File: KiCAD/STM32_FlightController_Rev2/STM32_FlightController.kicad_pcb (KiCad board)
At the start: 4 copper layers, 42 x 44.4 mm, 54 parts, among them J1 USB_B_Micro, J10 Conn_01x08_Pin, J19 Conn_02x05_Odd_Even, J2 Conn_01x04_Pin, J3 Conn_01x04_Pin, SW1 PTS815SJM, SW2 SW_SPDT, U1 USBLC6-2SC6, U2 AMS1117-3.3, U3 TLV70018, U4 STM32F405RGTx, U5 BMP390L, U6 ICM-20948, U7 SN74LVC1T45DBV, U8 SN74LVC1T45DBV, Y1 8MHz

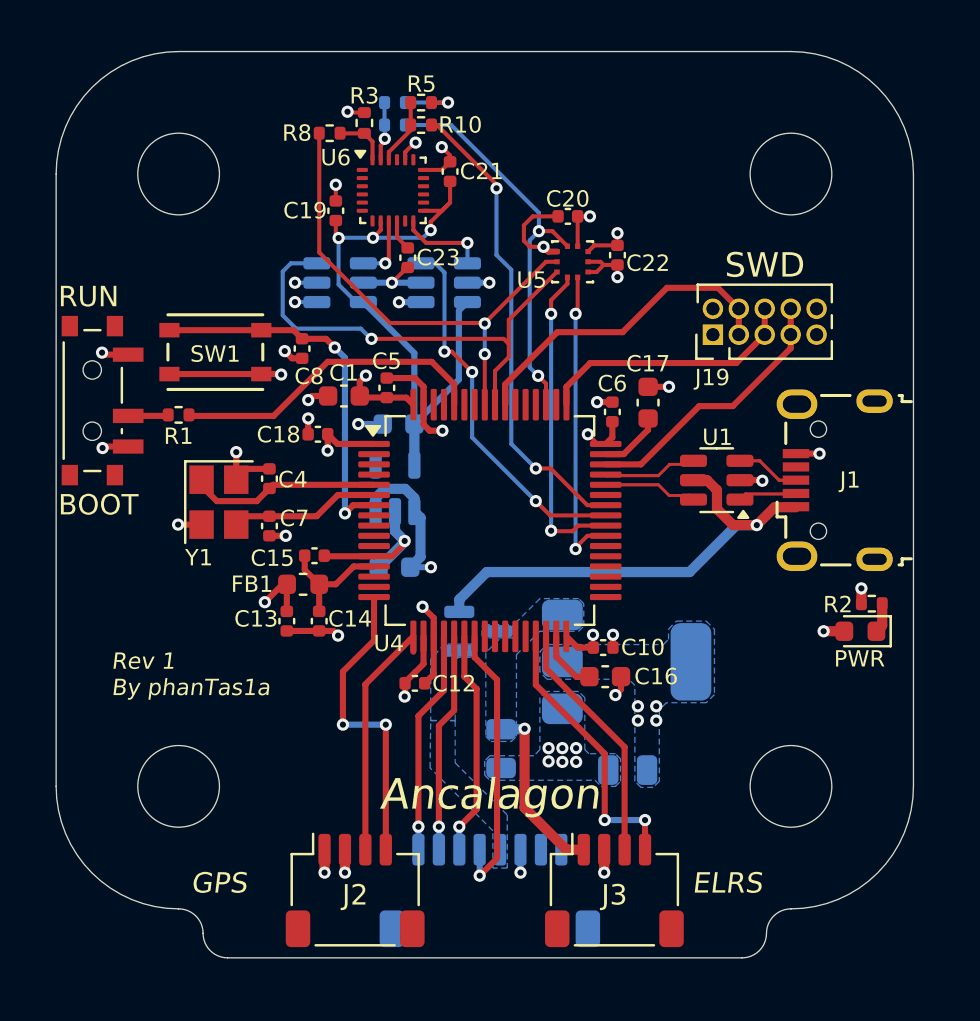
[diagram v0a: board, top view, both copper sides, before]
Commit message: adjusted mounting hole positions to 30.5mm apart
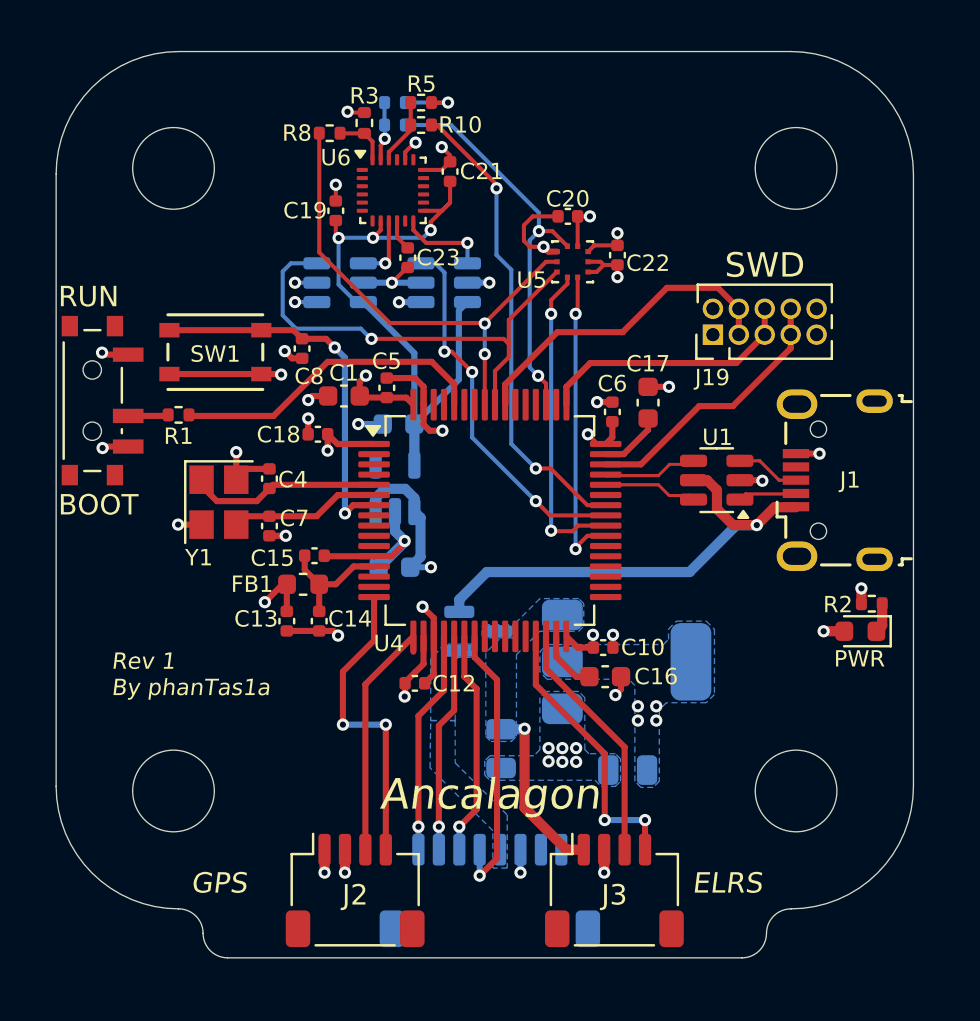
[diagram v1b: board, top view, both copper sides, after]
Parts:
- moved H1 0.37 mm to (99.5, 50.2)
- moved H2 0.37 mm to (130.0, 50.2)
- moved H3 0.34 mm to (99.5, 80.8)
- moved H4 0.34 mm to (130.0, 80.8)
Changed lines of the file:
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@@
 	(footprint "MountingHole:MountingHole_4mm"
 		(layer "F.Cu")
-		(at 99.75 50.525)
+		(at 99.5 50.25)
 		(descr "Mounting Hole 4mm, no annular")
 		(tags "mounting hole 4mm no annular")
@@
 	(footprint "MountingHole:MountingHole_4mm"
 		(layer "F.Cu")
-		(at 129.75 80.525)
+		(at 130 80.75)
 		(descr "Mounting Hole 4mm, no annular")
 		(tags "mounting hole 4mm no annular")
@@
 	(footprint "MountingHole:MountingHole_4mm"
 		(layer "F.Cu")
-		(at 129.75 50.525)
+		(at 130 50.25)
 		(descr "Mounting Hole 4mm, no annular")
 		(tags "mounting hole 4mm no annular")
@@
 	(footprint "MountingHole:MountingHole_4mm"
 		(layer "F.Cu")
-		(at 99.75 80.525)
+		(at 99.5 80.75)
 		(descr "Mounting Hole 4mm, no annular")
 		(tags "mounting hole 4mm no annular")

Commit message: various minor adjustments for positioning
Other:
- board text added: "X"
- board text added: "Y"
- board text added: "Z"

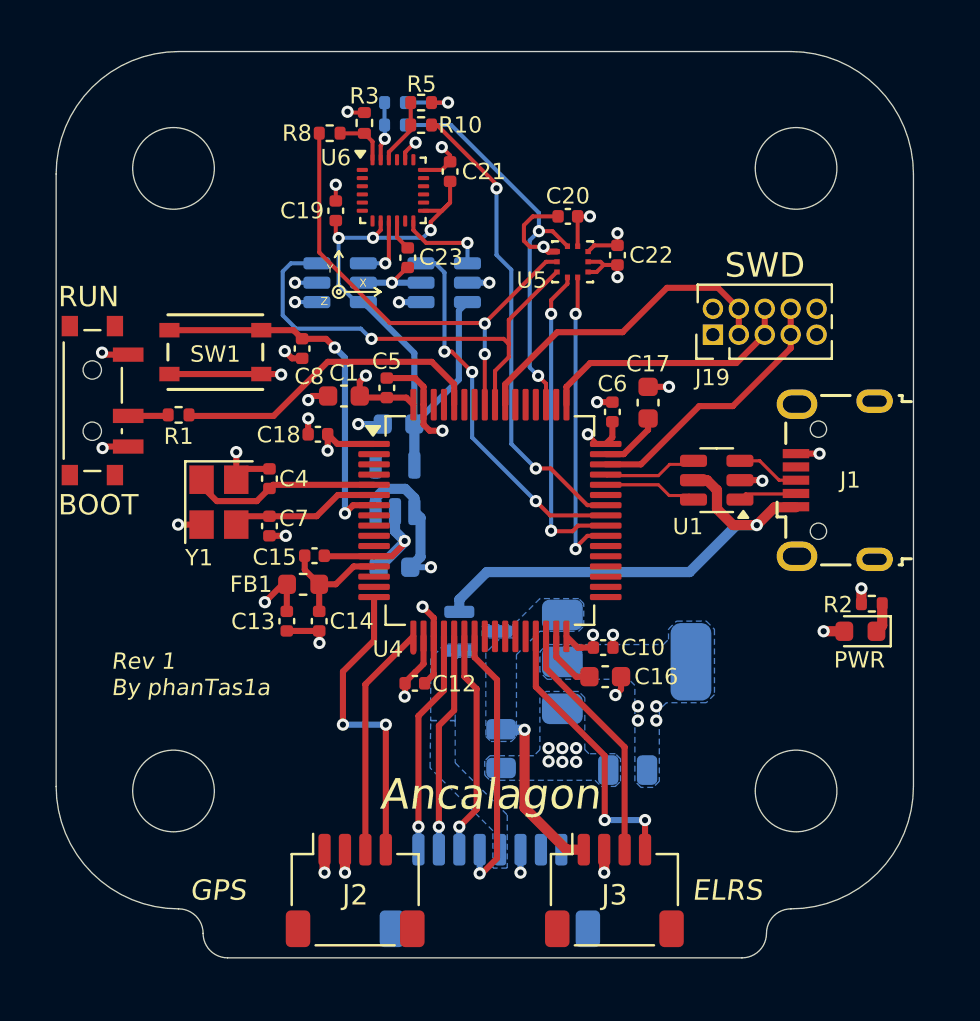
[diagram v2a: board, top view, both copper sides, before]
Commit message: finalizing components, adjusting some positioning
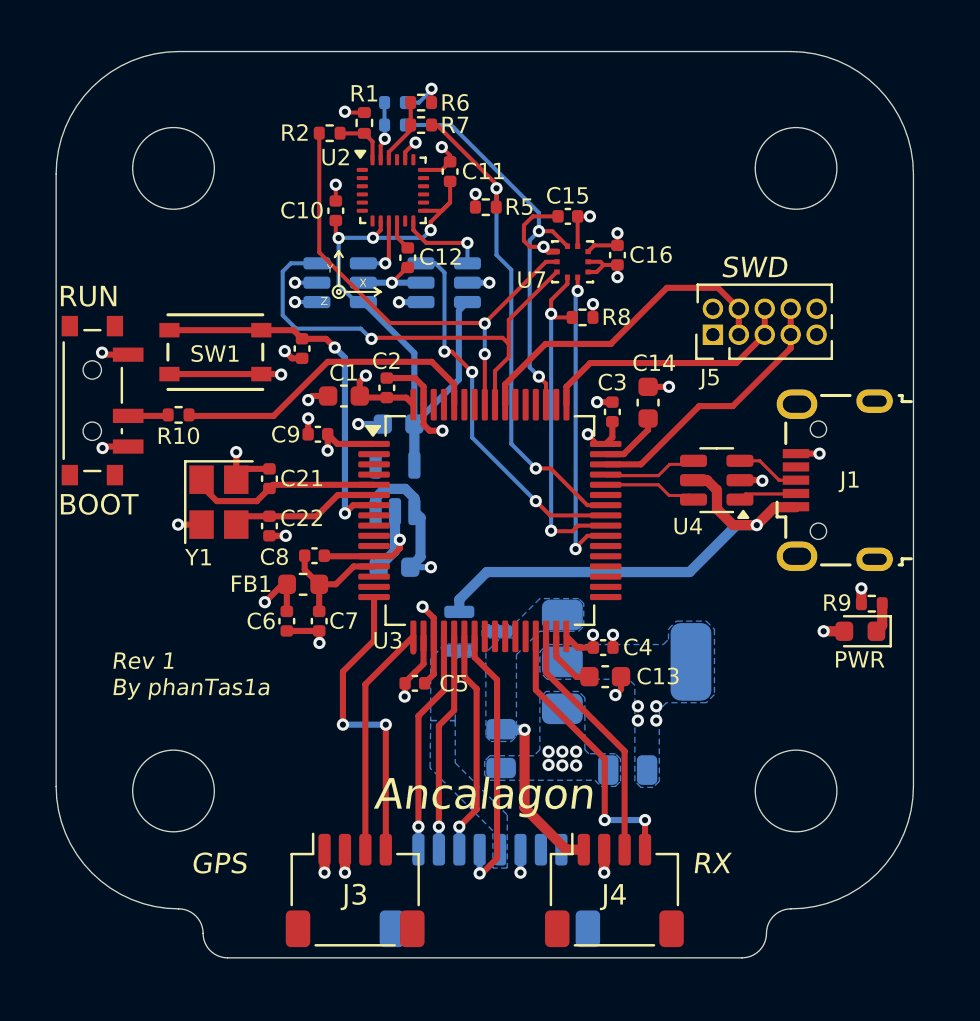
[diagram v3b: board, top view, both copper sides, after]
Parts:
- added R5: 10k, Resistor_SMD:R_0402_1005Metric, F.Cu at (114.8, 52.1)
- added R8: 10k, Resistor_SMD:R_0402_1005Metric, F.Cu at (119.5, 57.5)
- C21: renamed from C4; value 10p -> 14p
- C22: renamed from C7; value 10p -> 14p
- J1: value USB_B_Micro -> 629105150521
- J2: renamed from J10; value Conn_01x08_Pin -> JST_SH_SM08B-SRSS-TB_1x08-1MP_P1.00mm_Horizontal
- J3: renamed from J2; value Conn_01x04_Pin -> JST_SH_SM04B-SRSS-TB_1x04-1MP_P1.00mm_Horizontal
- J4: renamed from J3; value Conn_01x04_Pin -> JST_SH_SM04B-SRSS-TB_1x04-1MP_P1.00mm_Horizontal
- R1: renamed from R3; value 3.3k -> 3k3
- R2: renamed from R8; value 2.7k -> 2k7
- R3: renamed from R4; value 3.3k -> 2k7
- R4: renamed from R9; value 2.7k -> 2k7
- R6: renamed from R5; value 3.3k -> 3k3
- R7: renamed from R10; value 2.7k -> 2k7
- SW1: value PTS815SJM -> PTS815SJM250SMTRLFS
- SW2: value SW_SPDT -> PCM12SMTR
- Y1: value 8MHz -> X32258MOB4SI
- renumbered C19 to C10, C21 to C11, C23 to C12, C16 to C13, C17 to C14, C20 to C15, C22 to C16, C3 to C17, C9 to C18, C2 to C19, C5 to C2, C11 to C20, C8 to C23, C6 to C3, C10 to C4, C12 to C5, C13 to C6, C14 to C7, C15 to C8, C18 to C9, D2 to D1, D1 to D2, J19 to J5, R1 to R10, R2 to R9, U7 to U1, U6 to U2, U4 to U3, U1 to U4, U2 to U5, U3 to U6, U5 to U7
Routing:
- net +3V3: track 36.2 -> 37.5 mm, vias 18 -> 20
- net /CS2: track 15.5 -> 16.6 mm
- net /CS1: track 23.3 -> 24.2 mm
- net GND: track 65.4 -> 64.5 mm
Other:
- board text added: "RX"
- board text removed: "ELRS"

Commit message: replaced mounting holes with padded ones
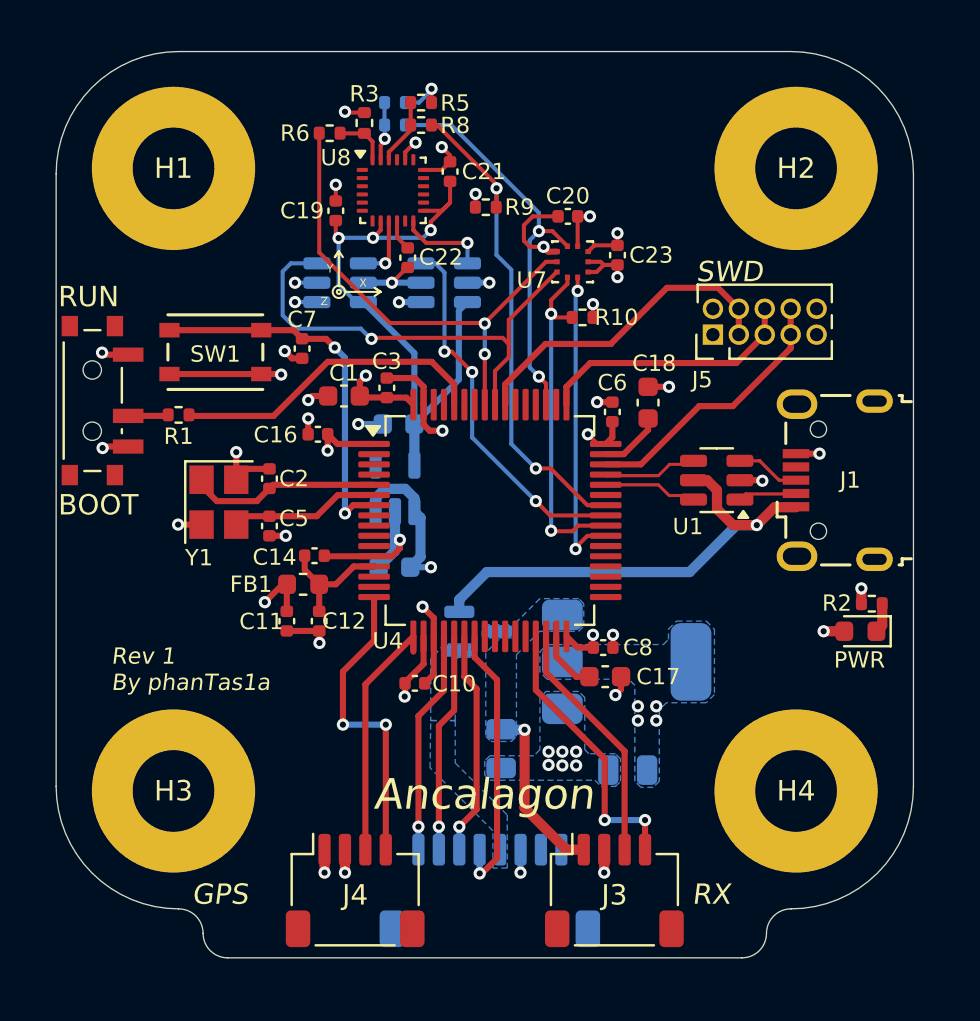
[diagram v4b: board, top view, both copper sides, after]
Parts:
- H1, H2, H3, H4: value MountingHole -> MountingHole_Pad; footprint MountingHole:MountingHole_4mm -> MountingHole:MountingHole_4mm_Pad
- renumbered C5 to C10, C6 to C11, C7 to C12, C17 to C13, C8 to C14, C18 to C15, C9 to C16, C13 to C17, C14 to C18, C10 to C19, C21 to C2, C15 to C20, C11 to C21, C12 to C22, C16 to C23, C2 to C3, C19 to C4, C22 to C5, C3 to C6, C23 to C7, C4 to C8, C20 to C9, D2 to D1, D1 to D2, J4 to J3, J3 to J4, R10 to R1, R8 to R10, R9 to R2, R1 to R3, R3 to R4, R6 to R5, R2 to R6, R4 to R7, R7 to R8, R5 to R9, U4 to U1, U5 to U2, U6 to U3, U3 to U4, U1 to U5, U8 to U6, U2 to U8

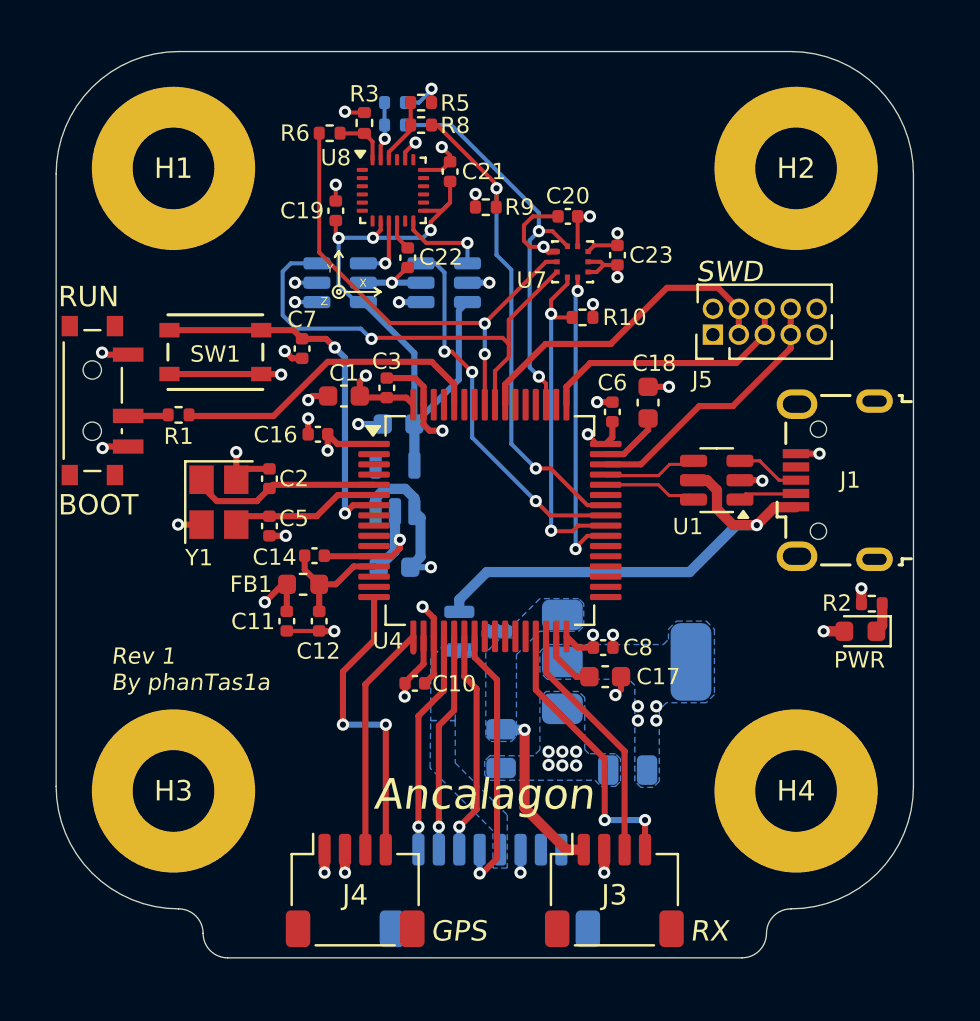
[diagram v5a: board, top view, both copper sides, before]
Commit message: cubeIDE code generation/setup
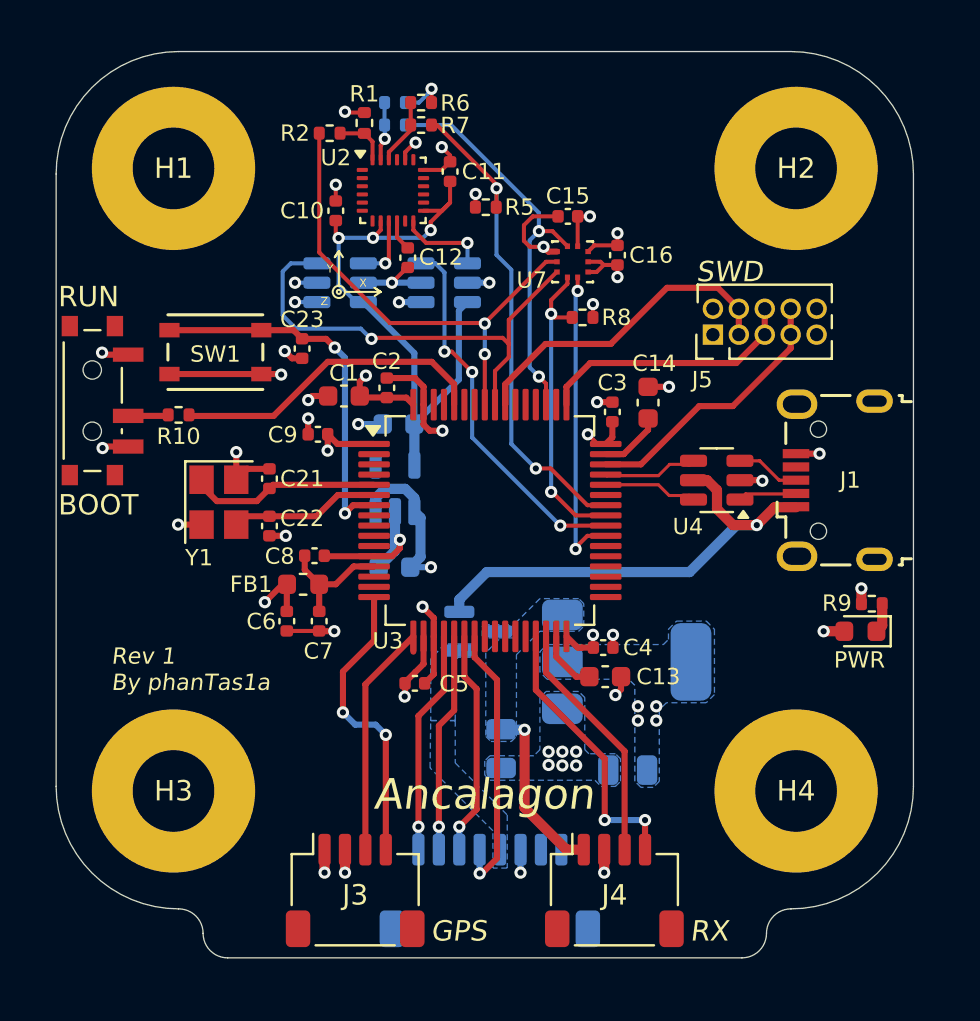
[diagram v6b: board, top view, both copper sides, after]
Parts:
- renumbered C19 to C10, C21 to C11, C22 to C12, C17 to C13, C18 to C14, C20 to C15, C23 to C16, C13 to C17, C15 to C18, C4 to C19, C3 to C2, C9 to C20, C2 to C21, C5 to C22, C7 to C23, C6 to C3, C8 to C4, C10 to C5, C11 to C6, C12 to C7, C14 to C8, C16 to C9, D2 to D1, D1 to D2, J4 to J3, J3 to J4, R3 to R1, R1 to R10, R6 to R2, R4 to R3, R7 to R4, R9 to R5, R5 to R6, R8 to R7, R10 to R8, R2 to R9, U5 to U1, U8 to U2, U4 to U3, U1 to U4, U2 to U5, U3 to U6, U6 to U8
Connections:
- U3 pad 40: /CS2 -> /INT1
- U3 pad 41: /INT1 -> /CS2
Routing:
- net /CS2: track 16.6 -> 15.1 mm
- net /GPS_RX: track 15.1 -> 14.5 mm

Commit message: swapped 5V and GND on the ELRS receiver connector
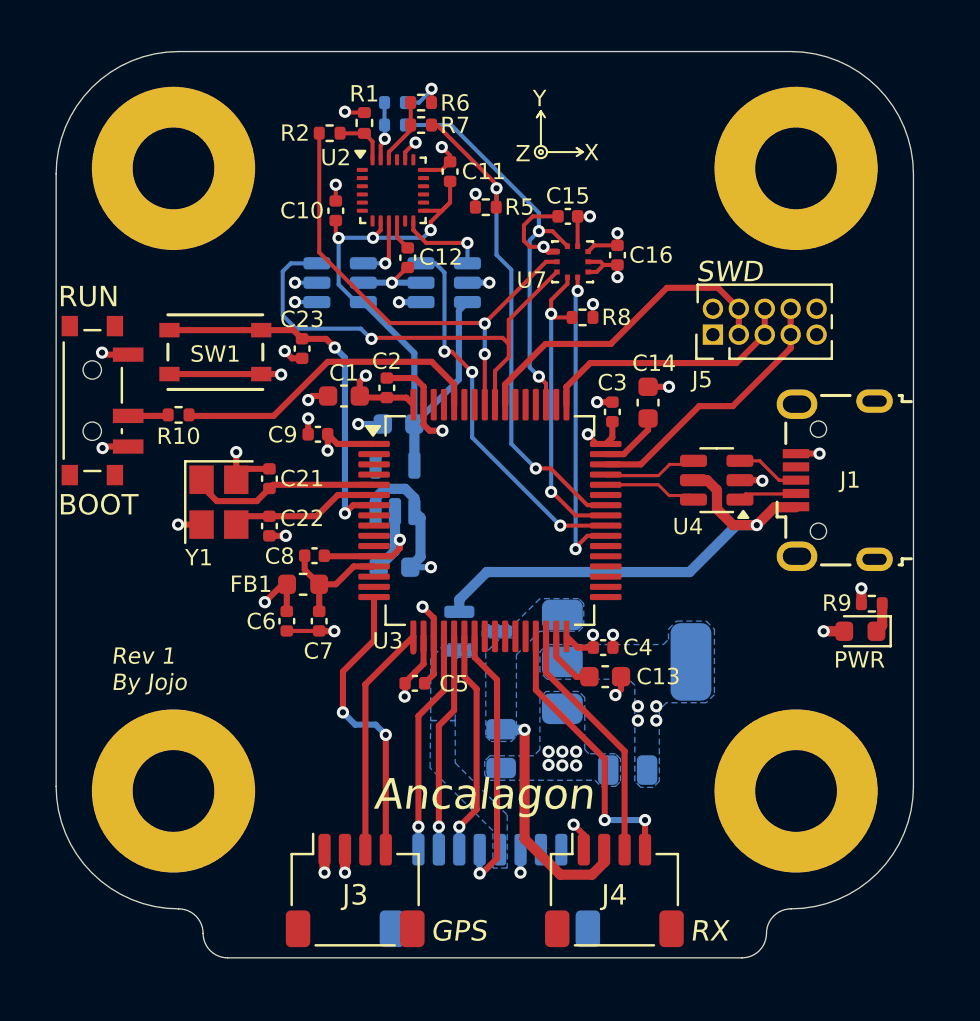
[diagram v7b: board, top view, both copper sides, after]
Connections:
- J4 pad 1: V_MAIN -> GND
- J4 pad 2: GND -> V_MAIN
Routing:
- net V_MAIN: track 8.73 -> 12.0 mm
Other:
- board text added: "Rev 1 By Jojo"
- board text removed: "Rev 1 By phanTas1a"

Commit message: added top, bottom ground planes w/ stitching
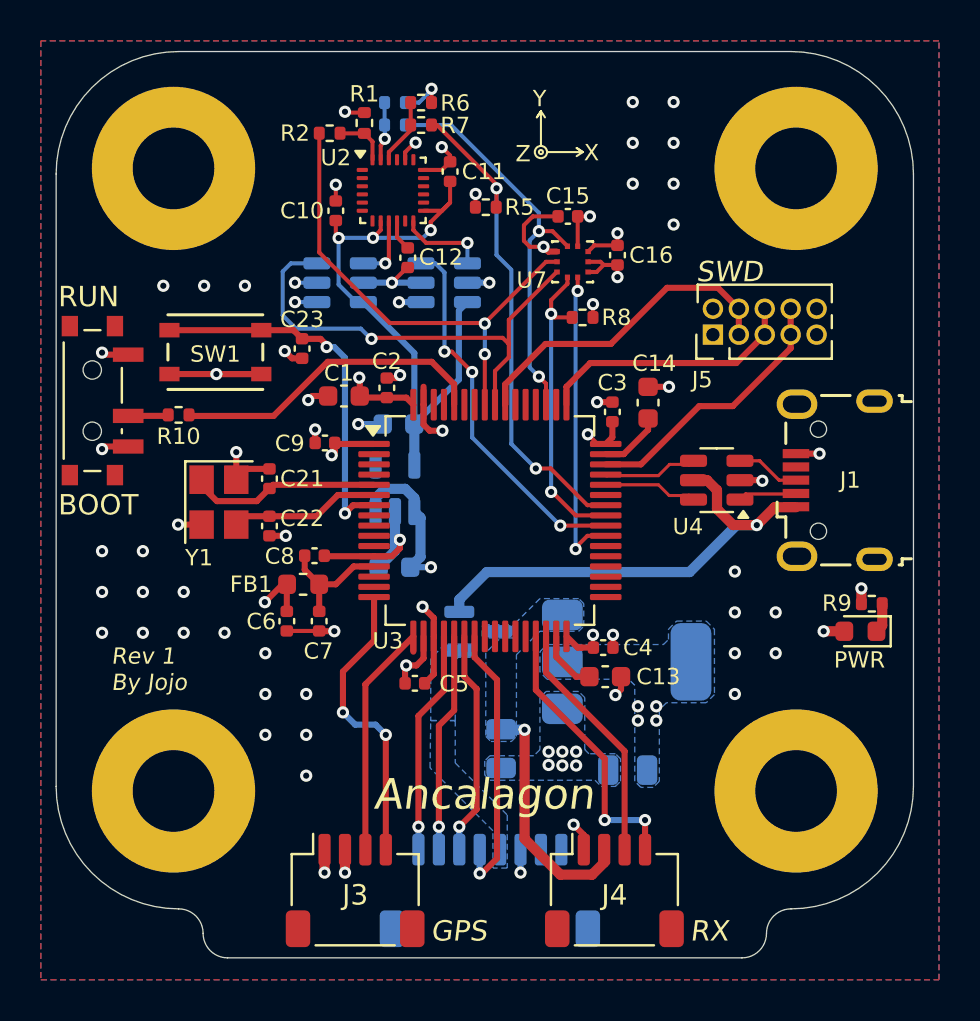
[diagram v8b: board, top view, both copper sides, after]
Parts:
- moved C9 0.55 mm to (106.9, 63.7)
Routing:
- net +3V3: track 37.5 -> 36.7 mm
- net GND: track 65.0 -> 64.5 mm, vias 39 -> 71
- added copper zone on F.Cu, net GND
